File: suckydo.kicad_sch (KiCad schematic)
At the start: 28 parts, among them J2 USB4105-GF-A, Q1 PJA3404A, Q2 MMBT2222A, U1 ESP32-C6-MINI-1-H4, U2 IP2721, U3 TPS25730D

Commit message: a bit more room
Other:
- note added: "PEDAL CONNECTION"
- moved on the sheet: C1, C2, C3, C4, D1, D2, Pedal, Q1, Q2, R1, R2, R3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

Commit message: ...and a small cleanup
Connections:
- net VCC is gone; now on net +3.3V: R6.1
- net VUSB renamed VBUS
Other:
- note removed: "IP2721 (simple)"
- note removed: "TPS25730DREFR (overkill?)"
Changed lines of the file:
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@@
 	(text "Push to reverse?"
 		(exclude_from_sim no)
-		(at 122.682 124.968 0)
-		(effects
-			(font
-				(size 1.27 1.27)
-			)
-		)
-	)
-	(text "TPS25730DREFR (overkill?)"
-		(exclude_from_sim no)
-		(at 43.18 89.154 0)
-		(effects
-			(font
-				(size 1.27 1.27)
-			)
-			(justify left)
+		(at 122.682 107.188 0)
+		(effects
+			(font
+				(size 1.27 1.27)
+			)
 		)
 	)
@@
 				(size 1.27 1.27)
 			)
-		)
-	)
-	(text "IP2721 (simple)"
-		(exclude_from_sim no)
-		(at 43.434 91.694 0)
-		(effects
-			(font
-				(size 1.27 1.27)
-			)
-			(justify left)
 		)
 	)
@@
 	)
 	(label "USB PD"
-		(at 43.18 87.63 0)
+		(at 60.96 87.63 0)
 		(fields_autoplaced yes)
 		(effects
@@
 	)
 	(label "USB-C 15V"
-		(at 24.13 87.63 0)
+		(at 41.91 87.63 0)
 		(fields_autoplaced yes)
 		(effects
@@
 	)
 	(label "ENCODER?"
-		(at 114.3 123.19 0)
+		(at 114.3 105.41 0)
 		(fields_autoplaced yes)
 		(effects
@@
 	)
 	(label "BUTTONS?"
-		(at 114.3 114.3 0)
+		(at 114.3 96.52 0)
 		(fields_autoplaced yes)
 		(effects
@@
 	)
 	(symbol
+		(lib_id "power:+3.3V")
+		(at 173.99 173.99 0)
+		(unit 1)
+		(exclude_from_sim no)
+		(in_bom yes)
+		(on_board yes)
+		(dnp no)
+		(fields_autoplaced yes)
+		(property "Reference" "#PWR011"
+			(at 173.99 177.8 0)
+			(effects
+				(font
+					(size 1.27 1.27)
+				)
+				(hide yes)
+			)
+		)
+		(property "Value" "+3.3V"
+			(at 173.99 168.91 0)
+			(effects
+				(font
+					(size 1.27 1.27)
+				)
+			)
+		)
+		(property "Footprint" ""
+			(at 173.99 173.99 0)
+			(effects
+				(font
+					(size 1.27 1.27)
+				)
+				(hide yes)
+			)
+		)
+		(property "Datasheet" ""
+			(at 173.99 173.99 0)
+			(effects
+				(font
+					(size 1.27 1.27)
+				)
+				(hide yes)
+			)
+		)
+		(property "Description" "Power symbol creates a global label with name \"+3.3V\""
+			(at 173.99 173.99 0)
+			(effects
+				(font
+					(size 1.27 1.27)
+				)
+				(hide yes)
+			)
+		)
+		(pin "1"
+		)
+		(instances
+			(project "suckydo"
+				(path "/c6a27179-ffbf-4c43-b356-2528cb51d20d"
+					(reference "#PWR011")
+					(unit 1)
+				)
+			)
+		)
+	)
+	(symbol
 		(lib_id "Device:C")
 		(at 30.48 40.64 0)
@@
 			)
 		)
-		(property "Value" "VUSB"
+		(property "Value" "VBUS"
 			(at 106.68 20.32 0)
 			(effects
@@
 					(unit 1)
 				)
-			)
-		)
-	)
-	(symbol
-		(lib_id "power:VCC")
-		(at 173.99 173.99 0)
-		(unit 1)
-		(exclude_from_sim no)
-		(in_bom yes)
-		(on_board yes)
-		(dnp no)
-		(fields_autoplaced yes)
-		(property "Reference" "#PWR011"
-			(at 173.99 177.8 0)
-			(effects
-				(font
-					(size 1.27 1.27)
-				)
-				(hide yes)
-			)
-		)
-		(property "Value" "VCC"
-			(at 173.99 170.18 0)
-			(effects
-				(font
-					(size 1.27 1.27)
-				)
-			)
-		)
-		(property "Footprint" ""
-			(at 173.99 173.99 0)
-			(effects
-				(font
-					(size 1.27 1.27)
-				)
-				(hide yes)
-			)
-		)
-		(property "Datasheet" ""
-			(at 173.99 173.99 0)
-			(effects
-				(font
-					(size 1.27 1.27)
-				)
-				(hide yes)
-			)
-		)
-		(property "Description" ""
-			(at 173.99 173.99 0)
-			(effects
-				(font
-					(size 1.27 1.27)
-				)
-				(hide yes)
-			)
-		)
-		(pin "1"
-		)
-		(instances
-			(project "suckydo"
-				(path "/c6a27179-ffbf-4c43-b356-2528cb51d20d"
-					(reference "#PWR011")
-					(unit 1)
-				)

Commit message: USB PD, MOSFET pump control, auto ESP boot mode
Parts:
- removed U2: IP2721, Package_SO:TSSOP-16_4.4x5mm_P0.65mm, symbol Interface_USB:IP2721
- added C10: 10u, Capacitor_SMD:C_0805_2012Metric, symbol Device:C
- added C7: 1u, Capacitor_SMD:C_0805_2012Metric, symbol Device:C
- added C8, C9: 100n, Capacitor_SMD:C_0805_2012Metric, symbol Device:C
- added D5: 1N4148, Diode_SMD:D_SOD-123, symbol Diode:1N4148
- added IC1: AP33771CFBZ-13-FA01, AP33771CFBZ13FA01, symbol Interface_USB:AP33771CFBZ-13-FA01
- added IC2: TS391SN2T1G, SOT95P275X110-5N, symbol Comparator:TS391SN2T1G
- added Pump: Screw_Terminal_01x02, symbol Connector:Screw_Terminal_01x02
- added Q3, Q4, Q6: PJA3404A, Package_TO_SOT_SMD:SOT-23, symbol Transistor_FET:IRLML0030
- added Q5: MMBT2222A, Package_TO_SOT_SMD:SOT-23, symbol Transistor_BJT:MMBT2222A
- added R11, R12: 0, Resistor_SMD:R_0805_2012Metric, symbol Device:R
- added R13: 52K, Resistor_SMD:R_0805_2012Metric, symbol Device:R
- added R14: 39K, Resistor_SMD:R_0805_2012Metric, symbol Device:R
- added R15: 100K, Resistor_SMD:R_0805_2012Metric, symbol Device:R
- added R16: 200K, Resistor_SMD:R_0805_2012Metric, symbol Device:R
- added R17, R18: 47k, Resistor_SMD:R_0805_2012Metric, symbol Device:R
- added R19: 5m, Resistor_SMD:R_0402_1005Metric, symbol Device:R
- added R20, R25: 100, Resistor_SMD:R_0805_2012Metric, symbol Device:R
- added R21: 10, Resistor_SMD:R_0805_2012Metric, symbol Device:R
- added R22: 1k, Resistor_SMD:R_0805_2012Metric, symbol Device:R
- added R23, R24: 10k, Resistor_SMD:R_0805_2012Metric, symbol Device:R
- added SW1: BOOT, symbol Switch:SW_Push
- added SW2: RESET, symbol Switch:SW_Push
- U3: now not fitted; now left out of the parts list
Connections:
- net +12V: now also D5.1 (K), Pump.1 (Pin_1), R24.2
- net +3.3V: now also R23.2
- net D+: now also R11.1
- net D-: now also R12.1
- net ESP_RESET: now also SW2.2
- net GND: now also C10.2, C7.2, C8.2, C9.2, IC1.15 (EP), IC1.5 (GND), IC2.2 (V-), Q5.2 (E), Q6.2 (S), R13.2, R14.2, R16.2, R18.1, SW1.1, SW2.1; no longer U3.28 (CC1), U3.29 (CC2)
- net IO9: now also IC2.1, R15.2, R16.1, SW1.2
- net VBUS: now also C10.1, IC1.4 (ISENP), R19.2
- net CC1: now reaches C5.1, J2.A5 (CC1), R7.2
- net CC1: now also IC1.11 (CC1)
- net CC2: now reaches C6.1, J2.B5 (CC2), R8.2
- net CC2: now also U3.28 (CC1), U3.29 (CC2), IC1.10 (CC2)
- net PUMP_CTRL: now reaches U1.9 (IO4)
- net PUMP_CTRL: now also R22.2
- new net: Q5.1 (B), R22.1, R23.1
- new net: C8.1, IC2.4 (+), R17.1, R18.2
- new net: IC1.9 (ISEL), R14.1
- new net: IC1.13 (DP), R11.2
- new net: Q6.1 (G), R25.2
- new net: IC1.1 (VOUT), R20.2
- new net: IC1.12 (DN), R12.2
- new net: Q3.1 (G), Q4.1 (G), R21.1
- new net: IC1.2 (PWR_EN), R21.2
- new net: Q5.3 (C), R24.1, R25.1
- new net: IC1.8 (VSEL), R13.1
- new net +5V: C7.1, C9.1, IC1.14 (V5V), IC2.3 (-), IC2.5 (V+), R15.1
- new net PUMP_LO: D5.2 (A), Pump.2 (Pin_2), Q6.3 (D)
- new net VBUS_SW: IC1.3 (VCC), Q3.2 (S), Q3.3 (D), Q4.2 (S), Q4.3 (D), R17.2, R19.1, R20.1
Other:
- note added: "+12V rail (min 2A) Quoi faire quand VBUS_SW est 5V au lieu de 15V?"
- note added: "+3.3V rail (min 500mA)"
- note added: "2.5V ou 7.5V"
- note added: "Ground IO9 si VBUS_SW = 5V"
- note added: "PUMP CONTROL"
- note added: "Try to negociate 15V 3A"
- note added: "Valider MOSFETs (temperature / puissance) Revoir IC pour timing (V5V, switch) LED?"
- note removed: "Boost converter from 5V?"
- note removed: "DRV8220"
- note removed: "Push to reverse?"
- note removed: "Resistances DNM pour TPS? Caps DNM pour IP2721?"
- moved on the sheet: C1, C2, C3, C4, C5, C6, D2, Pedal, R10, R5, R6, R7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

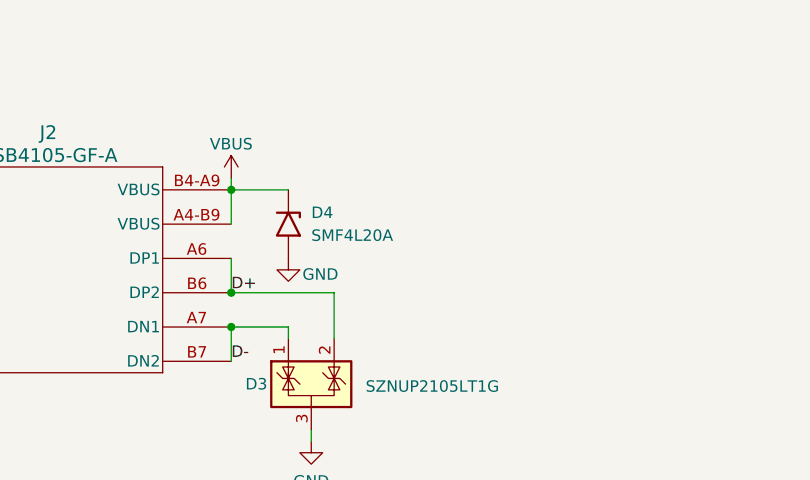
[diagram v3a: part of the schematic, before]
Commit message: note to check TVS on VBUS
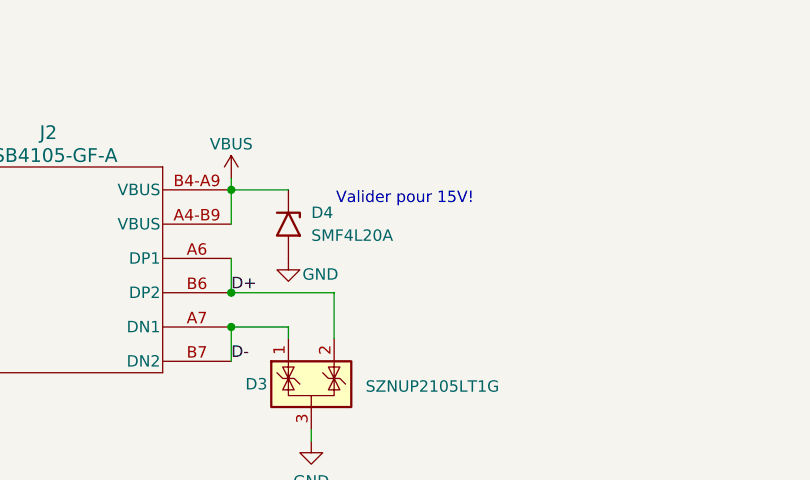
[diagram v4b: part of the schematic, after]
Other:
- note added: "Valider pour 15V!"
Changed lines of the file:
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@@
+		)
+	)
+	(text "Valider pour 15V!"
+		(exclude_from_sim no)
+		(at 125.984 26.416 0)
+		(effects
+			(font
+				(size 1.27 1.27)
+			)
 		)
 	)

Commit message: regulators
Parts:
- removed Q4: PJA3404A, Package_TO_SOT_SMD:SOT-23, symbol Transistor_FET:IRLML0030
- removed U3: TPS25730D, Package_DFN_QFN:Texas_REF0038A_WQFN-38-2EP_6x4mm_P0.4, symbol Interface_USB:TPS25730D
- added C11, C13, C15, C16, C18: 100n, Capacitor_SMD:C_0805_2012Metric, symbol Device:C
- added C12, C14, C17: 10u, Resistor_SMD:R_1210_3225Metric, symbol Device:C
- added C19: 47u, Capacitor_SMD:C_1206_3216Metric, symbol Device:C
- added IC3: TPS561201DDCR, SOT95P280X110-6N, symbol Regulator_Switching:TPS561201DDCR
- added L1: 1u, Inductor_SMD:XAL40XX, symbol Device:L
- added L2: L, Inductor_SMD:L_1008_2520Metric, symbol Device:L
- added PS1: TPS62135RGXR, TPS621361RGXT, symbol Regulator_Switching:TPS62135RGXR
- added R26, R27: 100k, Resistor_SMD:R_0805_2012Metric, symbol Device:R
- added R28: 1.62M, Resistor_SMD:R_0805_2012Metric, symbol Device:R
- added R29: 10K, Resistor_SMD:R_0805_2012Metric, symbol Device:R
- added R30: 33.2K, Resistor_SMD:R_0805_2012Metric, symbol Device:R
- added R31: 10k, Resistor_SMD:R_0805_2012Metric, symbol Device:R
- C10: footprint Capacitor_SMD:C_0805_2012Metric -> Resistor_SMD:R_1210_3225Metric
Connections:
- net +12V: now also C14.1, C15.1, C16.1, L1.2, PS1.6 (VOS), R26.1, R28.1
- net +3.3V: now also C19.1, L2.2, R30.1
- net +5V: now also C11.1
- net GND: now also C11.2, C12.2, C13.2, C14.2, C17.2, C19.2, IC3.1 (GND), PS1.10 (MODE), PS1.11 (VSEL), PS1.3 (GND), PS1.4 (FB_2), R27.2, R29.2, R31.2
- net PUMP_LO: now also C15.2
- net VALVE_LO: now also C16.2
- net VBUS_SW: now also C12.1, C17.1, IC3.3 (VIN), IC3.5 (EN), PS1.1 (VIN); no longer IC1.3 (VCC), Q3.3 (D), R19.1
- net 12V_EN: now reaches U1.12 (IO0)
- net 12V_EN: now also PS1.8 (EN), R29.1
- new net: PS1.5 (FB), R27.1, R28.2
- new net: C13.1, PS1.9 (SS/TR)
- new net: L1.1, PS1.2 (SW)
- new net: PS1.7 (PG), R26.2
- new net: IC3.4 (VFB), R30.2, R31.1
- new net: C18.2, IC3.2 (SW), L2.1
- new net: C18.1, IC3.6 (VBST)
- new net: IC1.3 (VCC), Q3.3 (D), R19.1
- no-connect marks 18 -> 17
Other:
- note added: "+12V rail (min 2A)"
- note added: "Boutons sur un board separe"
- note added: "Enlever le pullup sur IO9 et utiliser la sortie du comparateur?"
- note added: "RGB LED pour status? probleme USB, 12V disabled, etc?"
- note added: "Valider MOSFET (temperature, puissance)"
- note removed: "+12V rail (min 2A) Quoi faire quand VBUS_SW est 5V au lieu de 15V?"
- note removed: "Valider pour 15V!"
- moved on the sheet: C4, C9, D5, Pump, Q3, R10, Valve

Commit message: tweaks
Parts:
- removed D1, D5: 1N4148, Diode_SMD:D_SOD-123, symbol Diode:1N4148
- added D1, D5: SS210, Diode_SMD:D_SMA, symbol Diode:SS210
- added R32, R33: 47k, Resistor_SMD:R_0805_2012Metric, symbol Device:R
- L2: value L -> 3.3u
- R18: value 47k -> 23.2K
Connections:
- net +12V: now also D1.1 (K), D5.1 (K)
- net +5V: now also R32.1; no longer C9.1, IC2.3 (-)
- net GND: now also R33.2
- net PUMP_LO: now also D1.2 (A)
- net VALVE_LO: now also D5.2 (A)
- new net: C9.1, IC2.3 (-), R32.2, R33.1
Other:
- note added: "1.6 ou 5V"
- note added: "REVIEW - Don't exceed 5V on inputs?"
- note removed: "2.5V ou 7.5V"
- moved on the sheet: C8, C9

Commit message: double checked comparator
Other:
- note added: "LED?"
- note removed: "Enlever le pullup sur IO9 et utiliser la sortie du comparateur?"
- note removed: "REVIEW - Don't exceed 5V on inputs?"
- note removed: "Valider MOSFETs (temperature / puissance) Revoir IC pour timing (V5V, switch) LED?"
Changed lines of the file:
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@@
 		)
 	)
-	(text "Valider MOSFETs (temperature / puissance)\nRevoir IC pour timing (V5V, switch)\nLED?"
+	(text "LED?"
 		(exclude_from_sim no)
 		(at 62.484 67.31 0)
@@
 		)
 	)
-	(text "Enlever le pullup sur IO9 et utiliser la sortie du comparateur?"
-		(exclude_from_sim no)
-		(at 198.12 94.234 0)
-		(effects
-			(font
-				(size 1.27 1.27)
-			)
-		)
-	)
 	(text "Boutons sur un board separe"
 		(exclude_from_sim no)
@@
 		(effects
 			(font
-				(size 1.27 1.27)
-			)
-		)
-	)
-	(text "REVIEW - Don't exceed 5V on inputs?"
-		(exclude_from_sim no)
-		(at 107.95 71.374 0)
-		(effects
-			(font

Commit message: ui board connector and cleanup
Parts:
- removed SW1: BOOT, symbol Switch:SW_Push
- removed SW2: RESET, symbol Switch:SW_Push
- added J1: HFW14R-1STE1H1LF, HFW14R1STE1H1LF, symbol Connector:HFW14R-1STE1H1LF
- added R34, R35: 10K, Resistor_SMD:R_0805_2012Metric, symbol Device:R
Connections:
- net +3.3V: now also J1.14, R34.1, R35.1
- net ESP_RESET: now also J1.2
- net GND: now also J1.1, J1.11, J1.13, J1.3, J1.5, J1.7, J1.9, J1.MP1, J1.MP2
- net ESP_IO6: now reaches U1.15 (IO6)
- net ESP_IO6: now also J1.6
- net ESP_IO7: now reaches U1.16 (IO7)
- net ESP_IO7: now also J1.8
- net DISPLAY_SDA: now reaches U1.25 (IO19)
- net DISPLAY_SDA: now also J1.10, R34.2
- net DISPLAY_SCL: now reaches U1.26 (IO20)
- net DISPLAY_SCL: now also J1.12, R35.2
- net IO9 renamed ESP_BOOT
- net ESP_BOOT: now also J1.4; no longer IC2.1
- new net BOOT: IC2.1
- no-connect marks 17 -> 13
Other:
- note added: "12V RAIl"
- note added: "3.3V RAIL"
- note added: "ESP32-C6"
- note added: "UI BOARD CONNECTOR"
- note added: "USB IN"
- note added: "USB PD"
- note removed: "Bouton ou header pour programmer? Ou detection du voltage"
- moved on the sheet: C1, C10, C11, C12, C13, C14, C16, C17, C18, C19, C2, C3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
